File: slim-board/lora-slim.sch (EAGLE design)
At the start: 26 parts, among them IC1 STM32F030F4, IC2 ADP1607, J1 SWD_PTH_SHROUD, X1 SMA-142-0701-801/806, X2 UBLOX_MAX, X3 RFM98

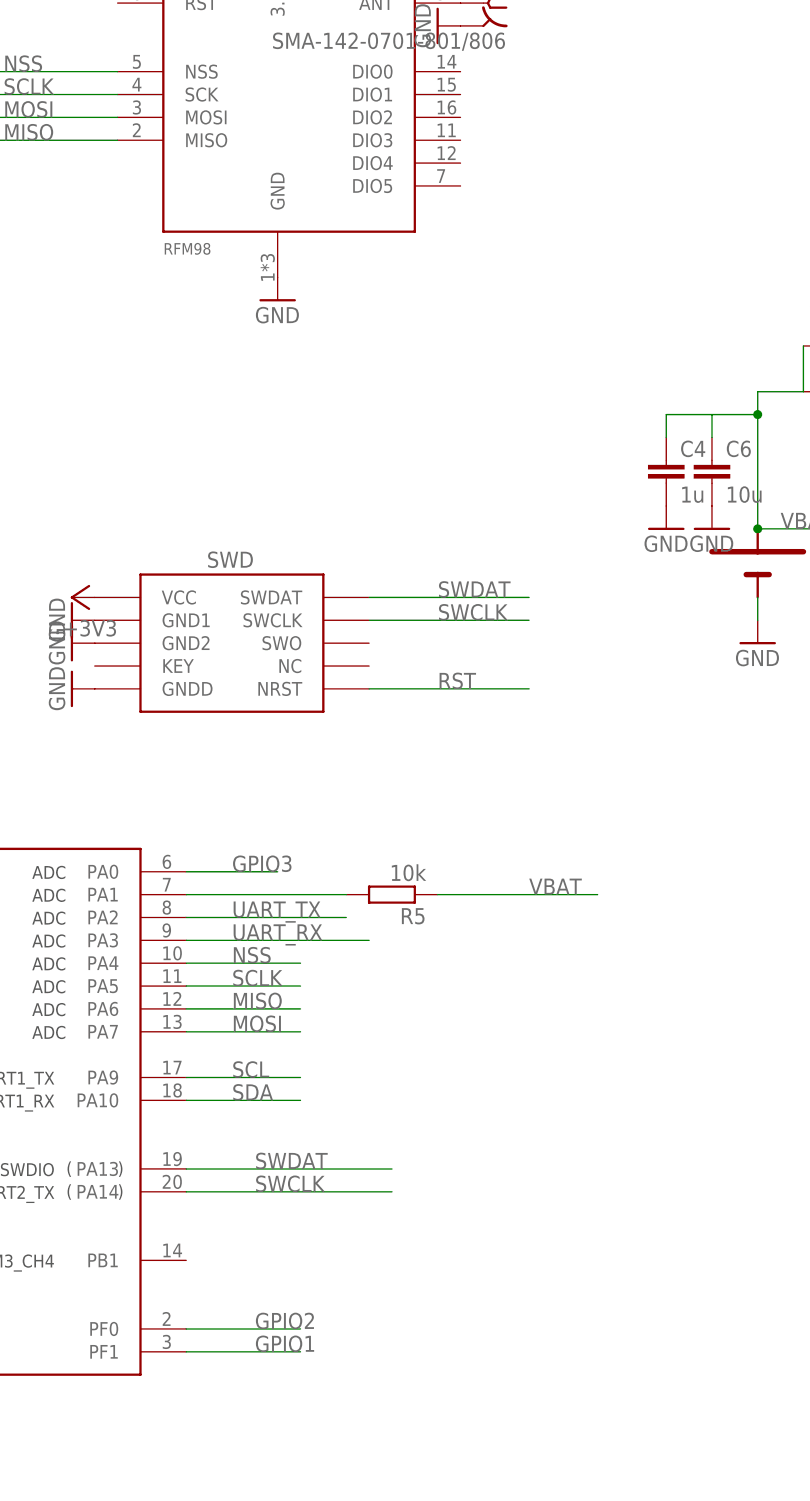
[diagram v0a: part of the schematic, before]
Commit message: connecting clkout
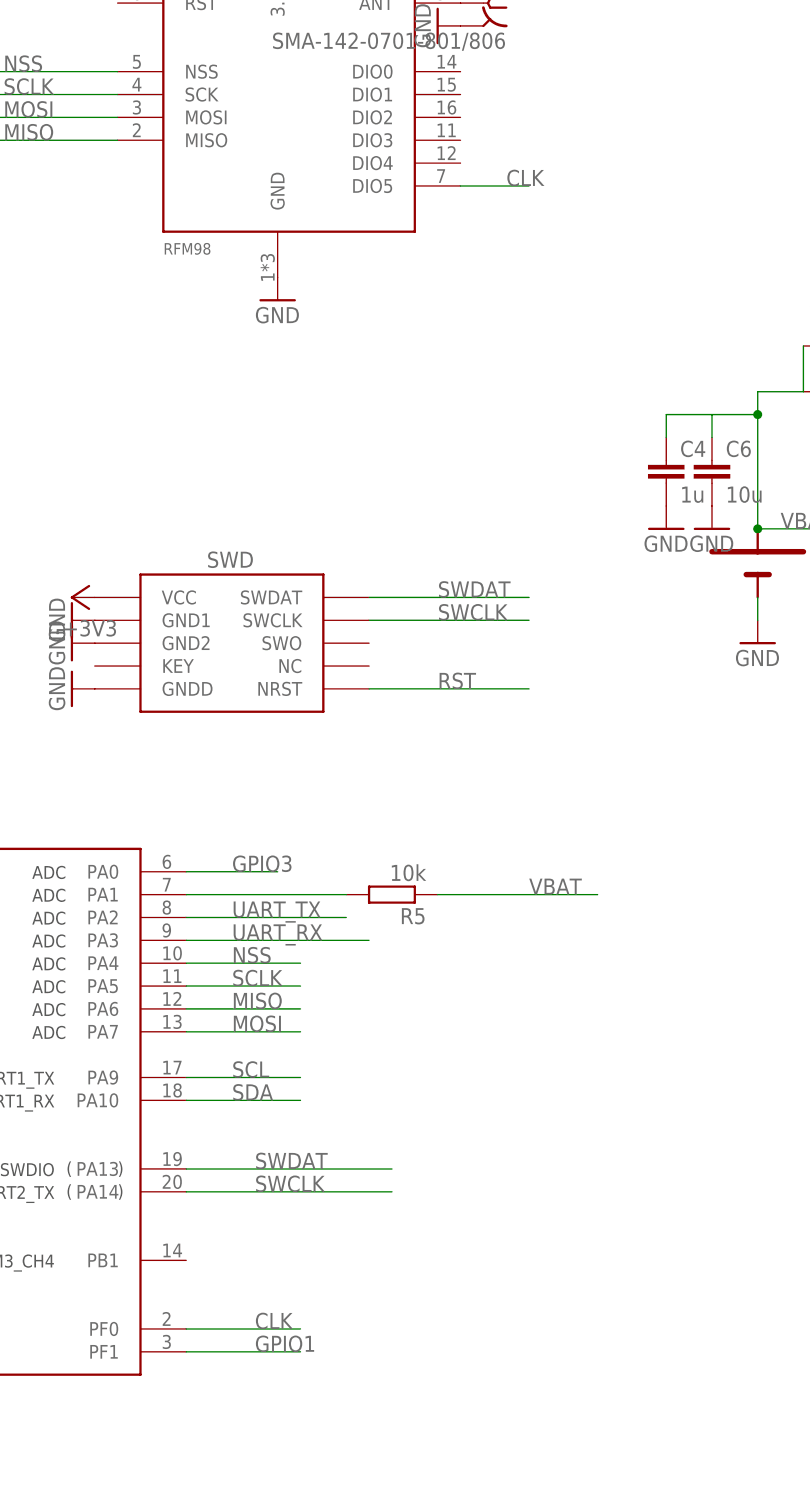
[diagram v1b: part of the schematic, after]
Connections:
- removed net GPIO2: IC1.PF0
- new net CLK: IC1.PF0, X3.DIO5
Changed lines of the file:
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@@
-</segment>
-</net>
-<net name="GPIO2" class="0">
-<segment>
-<label x="81.28" y="-20.32" size="1.778" layer="95"/>
-<wire x1="73.66" y1="-20.32" x2="86.36" y2="-20.32" width="0.1524" layer="91"/>
-<pinref part="IC1" gate="G$1" pin="PF0"/>
 </segment>
 </net>
@@
 </segment>
 </net>
+<net name="CLK" class="0">
+<segment>
+<pinref part="X3" gate="G$1" pin="DIO5"/>
+<wire x1="104.14" y1="106.68" x2="111.76" y2="106.68" width="0.1524" layer="91"/>
+<label x="109.22" y="106.68" size="1.778" layer="95"/>
+</segment>
+<segment>
+<label x="81.28" y="-20.32" size="1.778" layer="95"/>
+<wire x1="73.66" y1="-20.32" x2="86.36" y2="-20.32" width="0.1524" layer="91"/>
+<pinref part="IC1" gate="G$1" pin="PF0"/>
+</segment>
+</net>
